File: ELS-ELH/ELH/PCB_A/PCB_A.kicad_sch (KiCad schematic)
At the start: 40 parts, among them J1 Pressure Transducer Input, J2 Conn_01x09_Pin, J3 Conn_01x20_Pin, J4 Conn_01x20_Pin, Q1 IRLZ44N, Q2 IRLZ44N, Q4 IRLZ44N, Q6 IRLZ44N

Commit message: Update of 3D Models
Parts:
- removed J1: Pressure Transducer Input, TerminalBlock:TerminalBlock_MaiXu_MX126-5.0-03P_1x03_P5.00mm, symbol Connector:Screw_Terminal_01x03

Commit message: advances
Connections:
- net Ch_B_mosfet_1 is gone; now on net Ch_C_mosfet_1: R3.1
- net Ch_B_mosfet_2 is gone; now on net Ch_C_mosfet_2: R6.1
- net at Driver_DC2.4 (A01): now also Bornera1.2 (Pin_1); no longer Bornera1.1 (Pin_1)
- net at Driver_DC2.5 (A02): now also Bornera1.1 (Pin_2); no longer Bornera1.2 (Pin_2)
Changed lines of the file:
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@@
 		)
 	)
-	(label "Ch_B_mosfet_1"
+	(label "Ch_C_mosfet_1"
 		(at 26.67 118.11 180)
 		(effects
@@
 		)
 	)
-	(label "Ch_B_mosfet_2"
+	(label "Ch_C_mosfet_2"
 		(at 27.94 100.33 180)
 		(effects
@@
 	)
 	(symbol
-		(lib_name "Screw_Terminal_01x02_1")
+		(lib_name "Screw_Terminal_01x02_3")
 		(lib_id "Connector:Screw_Terminal_01x02")
 		(at 64.77 153.67 0)

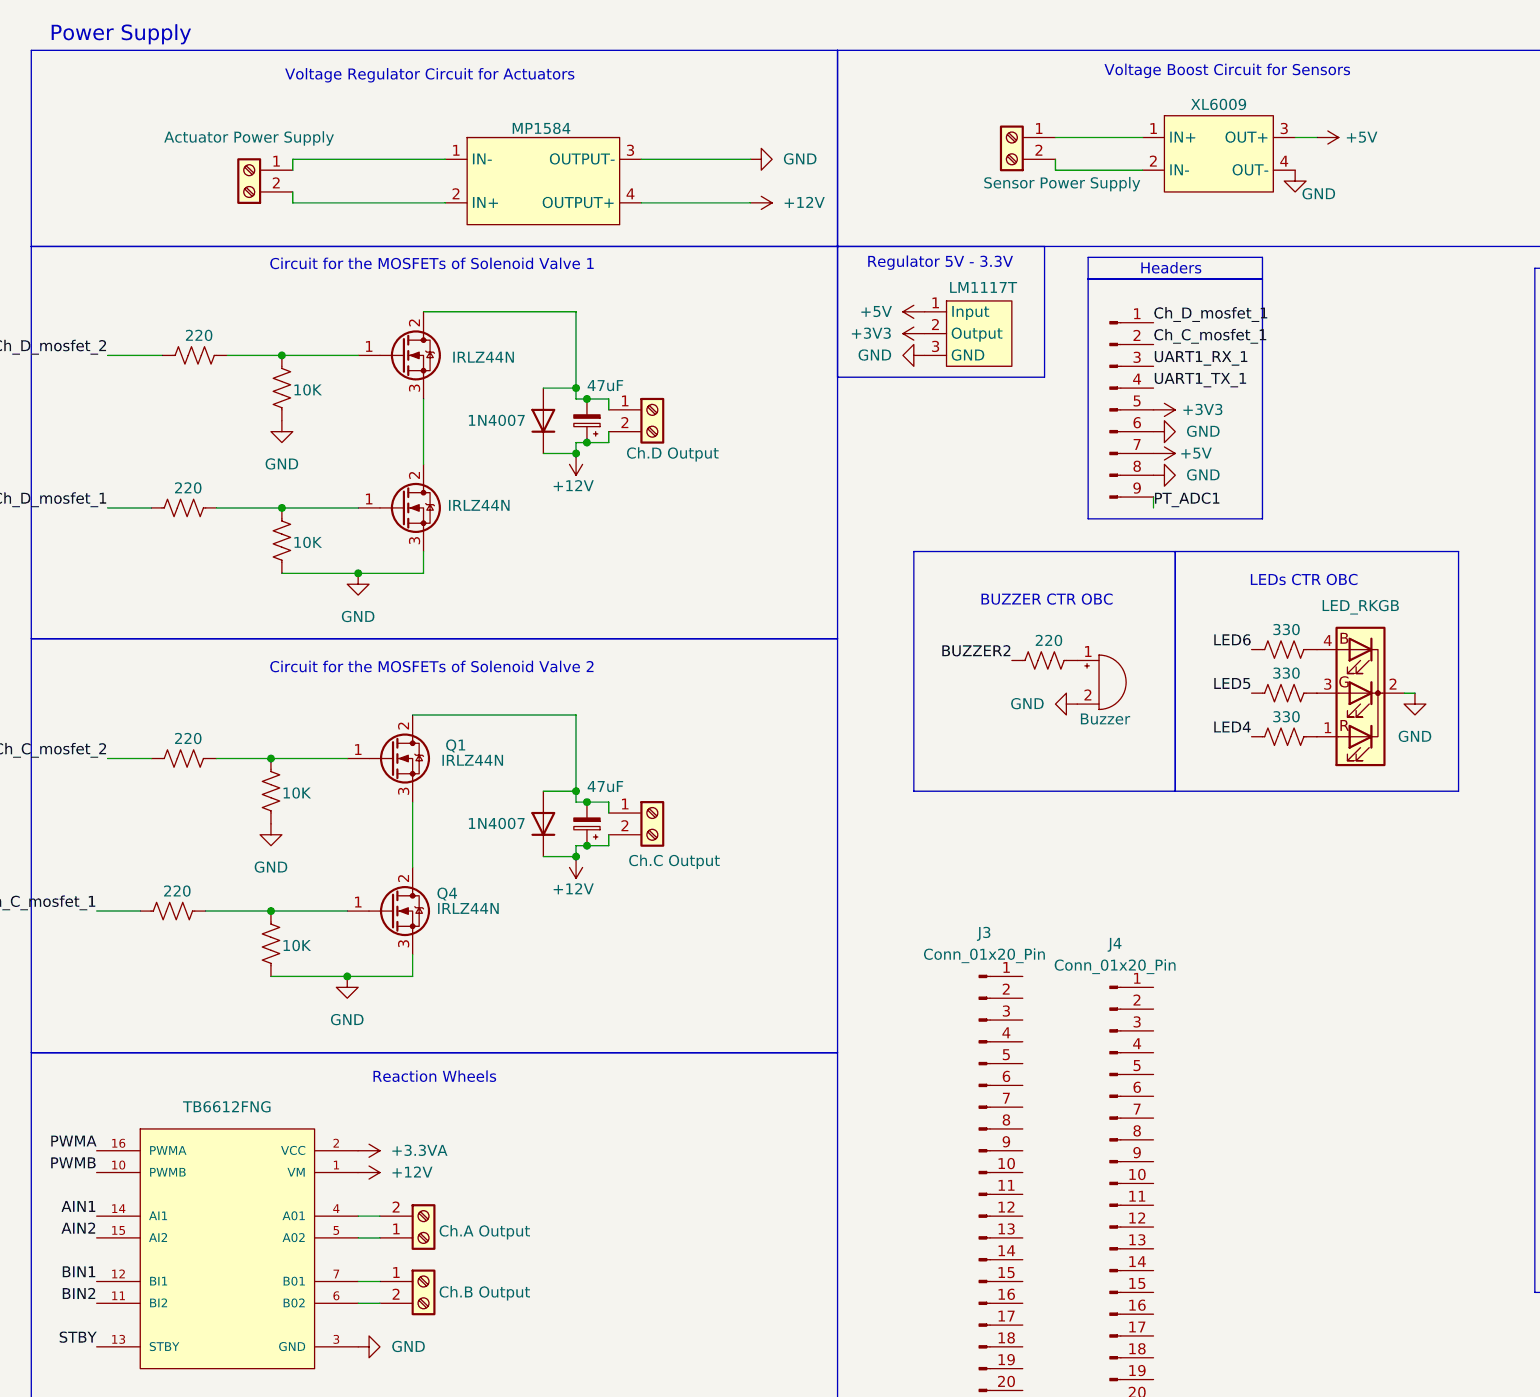
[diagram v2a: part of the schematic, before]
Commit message: Updates
The boost component was replaced, capacitors were added for the regulator, and the power supply voltage for the expansion module was changed
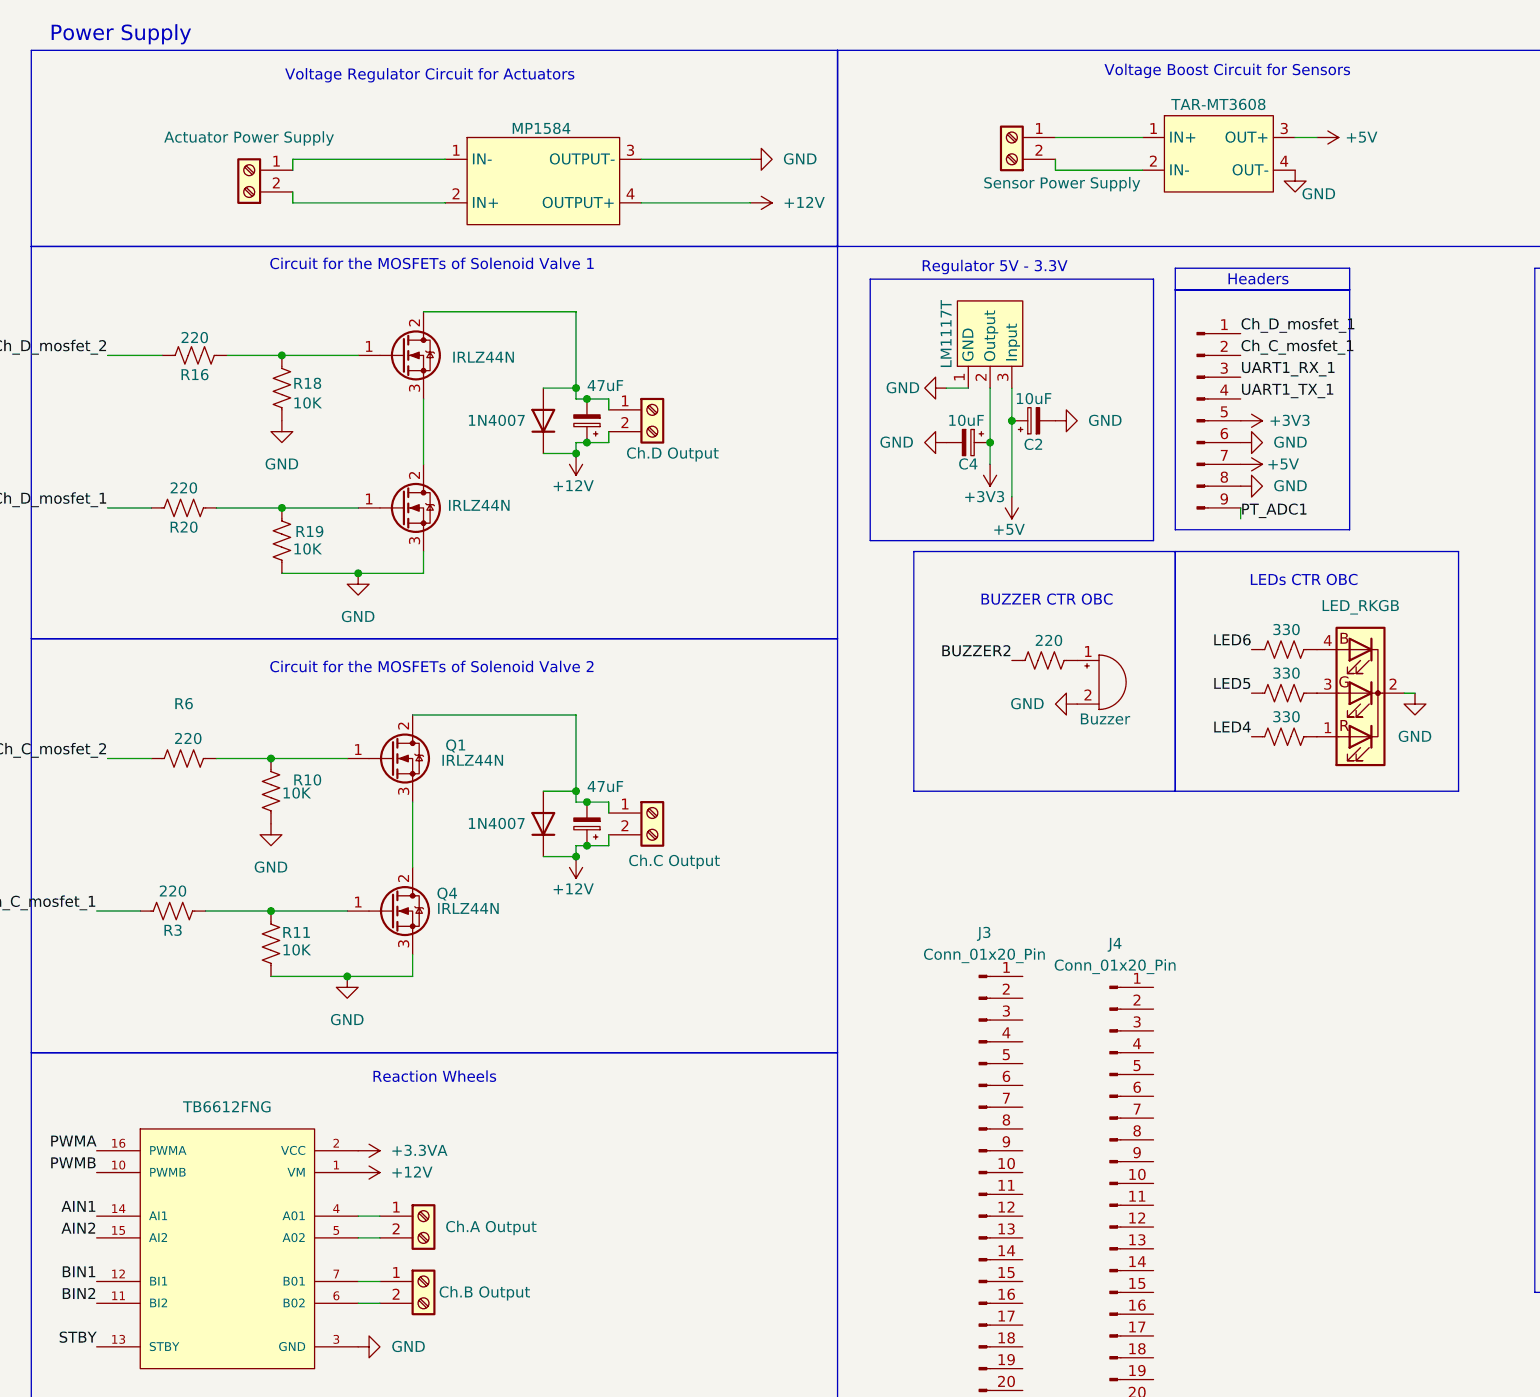
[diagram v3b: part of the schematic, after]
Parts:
- removed Bornera1: Ch.A Output, ELH_Library:Bornera 2P, symbol Connector:Screw_Terminal_01x02
- added Bornera2: Ch.A Output, ELH_Library:Bornera 2P, symbol Connector:Screw_Terminal_01x02
- added C2, C4: 10uF, Capacitor_THT:CP_Radial_D5.0mm_P2.00mm, symbol Device:C_Polarized_Small
- BOOST1: value XL6009 -> TAR-MT3608; footprint ELH_Library:XL6009 Boost -> ELH_Library:TAR-MT3608
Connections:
- net +3V3: now also C4.1
- net +5V: now also Regulator1.3 (Input), C2.1; no longer Regulator1.1 (Input)
- net GND: now also Regulator1.1 (GND), C2.2, C4.2; no longer Regulator1.3 (GND)
- net at Driver_DC2.4 (A01): now also Bornera2.1 (Pin_1)
- net at Driver_DC2.5 (A02): now also Bornera2.2 (Pin_2)

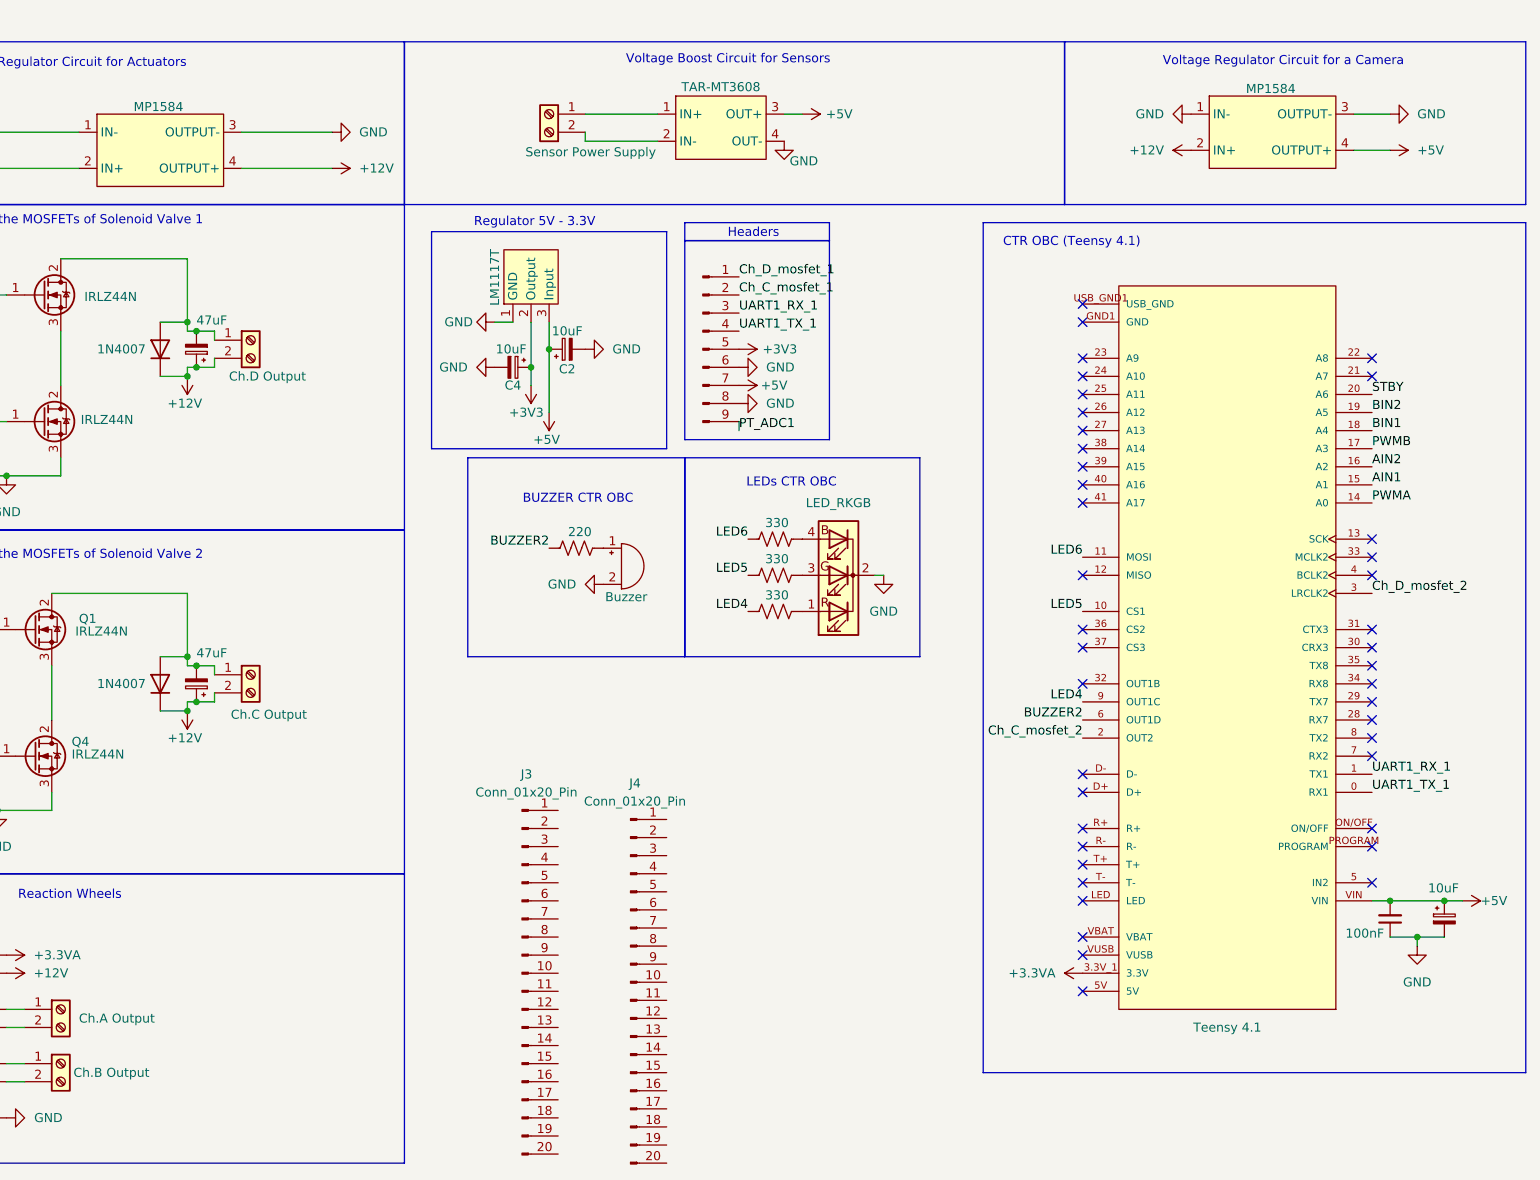
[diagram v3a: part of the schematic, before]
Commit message: preliminary PCB A connections
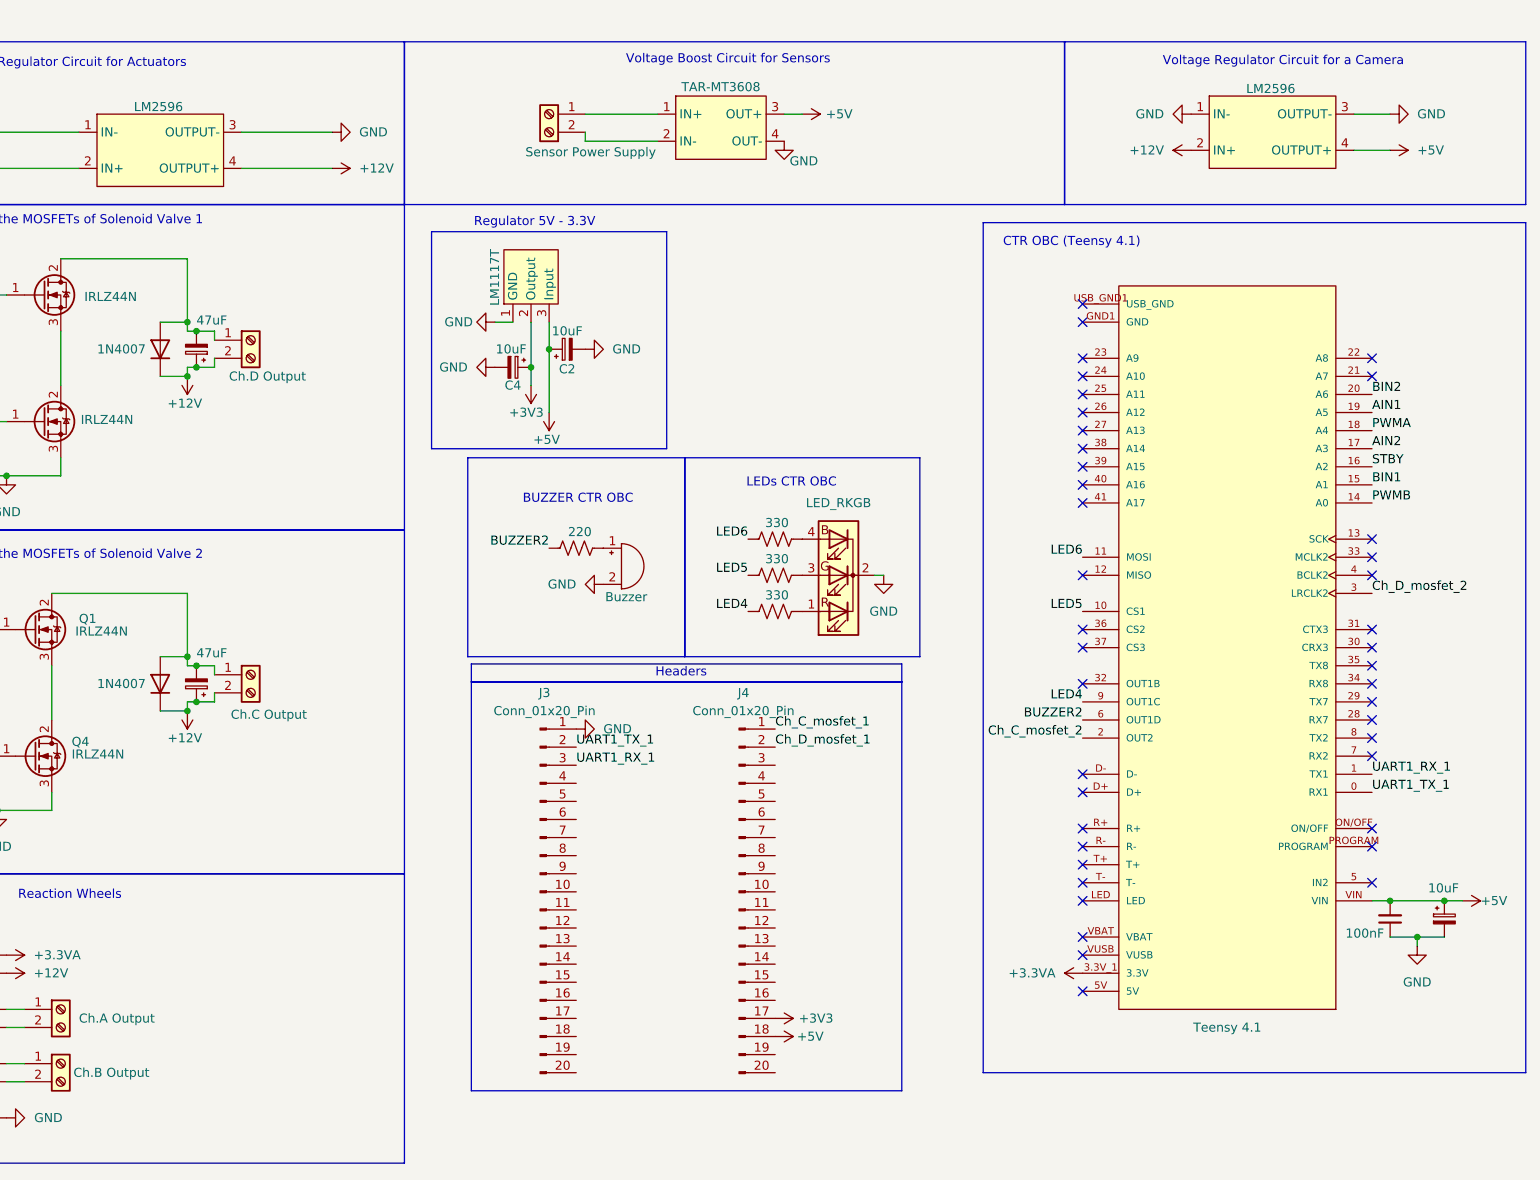
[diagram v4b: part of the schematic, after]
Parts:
- removed J2: Conn_01x09_Pin, Connector_Hirose:Hirose_DF13-09P-1.25DSA_1x09_P1.25mm_Vertical, symbol Connector:Conn_01x09_Pin
- Regulator3, Regulator4: value MP1584 -> LM2596; footprint ELH_Library:MP1584 -> ELH_Library:LM2596
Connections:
- net +3V3: now also J4.17 (Pin_17)
- net +5V: now also J4.18 (Pin_18)
- net AIN1: now also Teensy3.19 (A5); no longer Teensy3.15 (A1)
- net AIN2: now also Teensy3.17 (A3); no longer Teensy3.16 (A2)
- net BIN1: now also Teensy3.15 (A1); no longer Teensy3.18 (A4)
- net BIN2: now also Teensy3.20 (A6); no longer Teensy3.19 (A5)
- net Ch_C_mosfet_1: now also J4.1 (Pin_1)
- net Ch_D_mosfet_1: now also J4.2 (Pin_2)
- net GND: now also J3.1 (Pin_1)
- net PWMA: now also Teensy3.18 (A4); no longer Teensy3.14 (A0)
- net PWMB: now also Teensy3.14 (A0); no longer Teensy3.17 (A3)
- net STBY: now also Teensy3.16 (A2); no longer Teensy3.20 (A6)
- net UART1_RX_1: now also J3.3 (Pin_3)
- net UART1_TX_1: now also J3.2 (Pin_2)
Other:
- moved on the sheet: J3, J4

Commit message: PCB A advances
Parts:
- added BOOST2: TAR-MT3608, ELH_Library:TAR-MT3608, symbol ELH_Library:XL6009_Boost
- added Bornera1: Camera Connection, ELH_Library:Bornera 2P, symbol Connector:Screw_Terminal_01x02
- added Bornera8: Camera Power Supply, ELH_Library:Bornera 2P, symbol Connector:Screw_Terminal_01x02
- added J1: Conn_01x08_Pin, Connector_PinSocket_2.54mm:PinSocket_1x08_P2.54mm_Vertical, symbol Connector:Conn_01x08_Pin
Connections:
- net +3.3VA is gone; now on net +3V3: Driver_DC2.2 (VCC), Teensy3.3.3V_1 (3.3V), Teensy3.3.3V_2 (3.3V), Teensy3.3.3V_3 (3.3V)
- net +3V3: now also J4.13 (Pin_13); no longer J4.17 (Pin_17)
- net +5V: now also J4.14 (Pin_14), J1.1 (Pin_1); no longer J4.18 (Pin_18)
- net Ch_C_mosfet_1: now also J4.7 (Pin_7), J4.8 (Pin_8), J4.9 (Pin_9); no longer J4.1 (Pin_1)
- net Ch_C_mosfet_2: now also Teensy3.22 (A8); no longer Teensy3.2 (OUT2)
- net Ch_D_mosfet_1: now also J4.18 (Pin_18), J4.19 (Pin_19), J4.20 (Pin_20); no longer J4.2 (Pin_2)
- net Ch_D_mosfet_2: now also Teensy3.36 (CS2); no longer Teensy3.3 (LRCLK2)
- net GND: now also BOOST1.2 (IN-), Bornera3.1 (Pin_2), Bornera6.2 (Pin_1), Regulator4.1 (IN-), BOOST2.2 (IN-), BOOST2.4 (OUT-), Bornera1.1 (Pin_2), Bornera8.2 (Pin_1), J1.2 (Pin_2)
- net LED4: now also Teensy3.11 (MOSI); no longer Teensy3.9 (OUT1C)
- net LED6: now also Teensy3.9 (OUT1C); no longer Teensy3.11 (MOSI)
- net UART1_RX_1: now also J3.5 (Pin_5), J3.6 (Pin_6), J3.7 (Pin_7), Teensy3.4 (BCLK2); no longer J3.3 (Pin_3), Teensy3.1 (TX1)
- net UART1_TX_1: now also J3.3 (Pin_3), J3.4 (Pin_4)
- net LPWM: now reaches Teensy3.13 (SCK)
- net LPWM: now also J1.8 (Pin_8)
- net RPWM: now reaches Teensy3.41 (A17)
- net RPWM: now also J1.7 (Pin_7)
- new net: BOOST2.3 (OUT+), Bornera1.2 (Pin_1)
- new net: BOOST2.1 (IN+), Bornera8.1 (Pin_2)
- new net L_EN: J1.6 (Pin_6)
- new net L_IS: J1.4 (Pin_4)
- new net R_EN: J1.5 (Pin_5)
- new net R_IS: J1.3 (Pin_3)
- no-connect marks 41 -> 39
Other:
- note added: "Voltage Boost Circuit for Camera"
- note added: "Voltage Regulator Circuit for LM1117T"
- note removed: "Voltage Regulator Circuit for a Camera"
